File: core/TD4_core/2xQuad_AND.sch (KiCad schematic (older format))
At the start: 2 parts, among them U18 74HC21

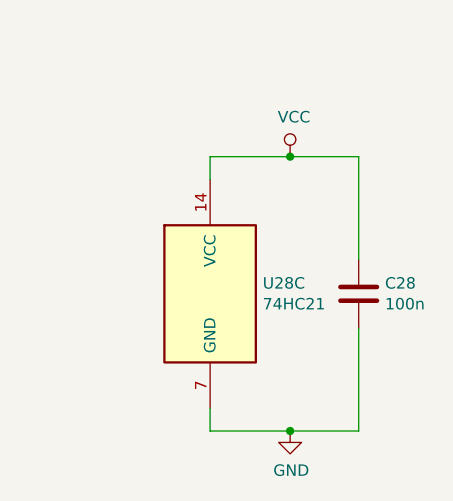
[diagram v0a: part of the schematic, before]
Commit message: Core schematic done. Backplane connector added, including separate .sch file to append.
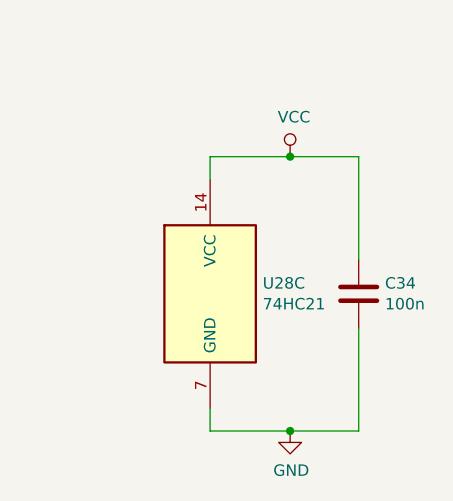
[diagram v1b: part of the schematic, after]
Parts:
- C24: renamed from C18; footprint (none) -> Capacitor_SMD:C_0805_2012Metric
- U18: footprint (none) -> Package_SO:SOIC-14_3.9x8.7mm_P1.27mm
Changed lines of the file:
@@
 encoding utf-8
 Sheet 7 23
-Title ""
+Title "TD4 core module"
 Date ""
-Rev ""
+Rev "v1.0"
 Comp ""
 Comment1 ""
@@
 F 0 "U28" H 4950 2875 50  0000 C CNN
 F 1 "74HC21" H 4950 2784 50  0000 C CNN
-F 2 "" H 4950 2500 50  0001 C CNN
+F 2 "Package_SO:SOIC-14_3.9x8.7mm_P1.27mm" H 4950 2500 50  0001 C CNN
 F 3 "http://www.ti.com/lit/gpn/sn74LS21" H 4950 2500 50  0001 C CNN
 	1    4950 2500
@@
 F 0 "U28" H 4950 3925 50  0000 C CNN
 F 1 "74HC21" H 4950 3834 50  0000 C CNN
-F 2 "" H 4950 3550 50  0001 C CNN
+F 2 "Package_SO:SOIC-14_3.9x8.7mm_P1.27mm" H 4950 3550 50  0001 C CNN
 F 3 "http://www.ti.com/lit/gpn/sn74LS21" H 4950 3550 50  0001 C CNN
 	2    4950 3550
@@
 F 0 "U28" H 8280 5546 50  0000 L CNN
 F 1 "74HC21" H 8280 5455 50  0000 L CNN
-F 2 "" H 8050 5500 50  0001 C CNN
+F 2 "Package_SO:SOIC-14_3.9x8.7mm_P1.27mm" H 8050 5500 50  0001 C CNN
 F 3 "http://www.ti.com/lit/gpn/sn74LS21" H 8050 5500 50  0001 C CNN
 	3    8050 5500
@@
 AR Path="/5C5DC05E/5CD3CB5B/5C84DA33" Ref="C?"  Part="1"
 AR Path="/5C5DC05E/5CD3CB61/5C84DA33" Ref="C?"  Part="1"
-AR Path="/5C594F41/5C66871A/5C84DA33" Ref="C18"  Part="1"
+AR Path="/5C594F41/5C66871A/5C84DA33" Ref="C24"  Part="1"
 AR Path="/5C594F41/5C66DC99/5C84DA33" Ref="C?"  Part="1"
-AR Path="/5C594F41/5C66DD80/5C84DA33" Ref="C25"  Part="1"
-AR Path="/5C594F41/5C676674/5C84DA33" Ref="C28"  Part="1"
-F 0 "C28" H 8815 5546 50  0000 L CNN
+AR Path="/5C594F41/5C66DD80/5C84DA33" Ref="C31"  Part="1"
+AR Path="/5C594F41/5C676674/5C84DA33" Ref="C34"  Part="1"
+F 0 "C34" H 8815 5546 50  0000 L CNN
 F 1 "100n" H 8815 5455 50  0000 L CNN
-F 2 "" H 8738 5350 50  0001 C CNN
+F 2 "Capacitor_SMD:C_0805_2012Metric" H 8738 5350 50  0001 C CNN
 F 3 "~" H 8700 5500 50  0001 C CNN
 	1    8700 5500
@@
 AR Path="/5C5DC05E/5CD3CB5B/5C84DB98" Ref="#PWR?"  Part="1"
 AR Path="/5C5DC05E/5CD3CB61/5C84DB98" Ref="#PWR?"  Part="1"
-AR Path="/5C594F41/5C66871A/5C84DB98" Ref="#PWR062"  Part="1"
+AR Path="/5C594F41/5C66871A/5C84DB98" Ref="#PWR076"  Part="1"
 AR Path="/5C594F41/5C66DC99/5C84DB98" Ref="#PWR?"  Part="1"
-AR Path="/5C594F41/5C66DD80/5C84DB98" Ref="#PWR082"  Part="1"
-AR Path="/5C594F41/5C676674/5C84DB98" Ref="#PWR090"  Part="1"
-F 0 "#PWR090" H 8400 5850 50  0001 C CNN
+AR Path="/5C594F41/5C66DD80/5C84DB98" Ref="#PWR096"  Part="1"
+AR Path="/5C594F41/5C676674/5C84DB98" Ref="#PWR0104"  Part="1"
+F 0 "#PWR0104" H 8400 5850 50  0001 C CNN
 F 1 "GND" H 8405 5927 50  0000 C CNN
 F 2 "" H 8400 6100 50  0001 C CNN
@@
 AR Path="/5C5DC05E/5CD3CB5B/5C84DC2A" Ref="#PWR?"  Part="1"
 AR Path="/5C5DC05E/5CD3CB61/5C84DC2A" Ref="#PWR?"  Part="1"
-AR Path="/5C594F41/5C66871A/5C84DC2A" Ref="#PWR061"  Part="1"
+AR Path="/5C594F41/5C66871A/5C84DC2A" Ref="#PWR075"  Part="1"
 AR Path="/5C594F41/5C66DC99/5C84DC2A" Ref="#PWR?"  Part="1"
-AR Path="/5C594F41/5C66DD80/5C84DC2A" Ref="#PWR081"  Part="1"
-AR Path="/5C594F41/5C676674/5C84DC2A" Ref="#PWR089"  Part="1"
-F 0 "#PWR089" H 8400 4750 50  0001 C CNN
+AR Path="/5C594F41/5C66DD80/5C84DC2A" Ref="#PWR095"  Part="1"
+AR Path="/5C594F41/5C676674/5C84DC2A" Ref="#PWR0103"  Part="1"
+F 0 "#PWR0103" H 8400 4750 50  0001 C CNN
 F 1 "VCC" H 8417 5073 50  0000 C CNN
 F 2 "" H 8400 4900 50  0001 C CNN

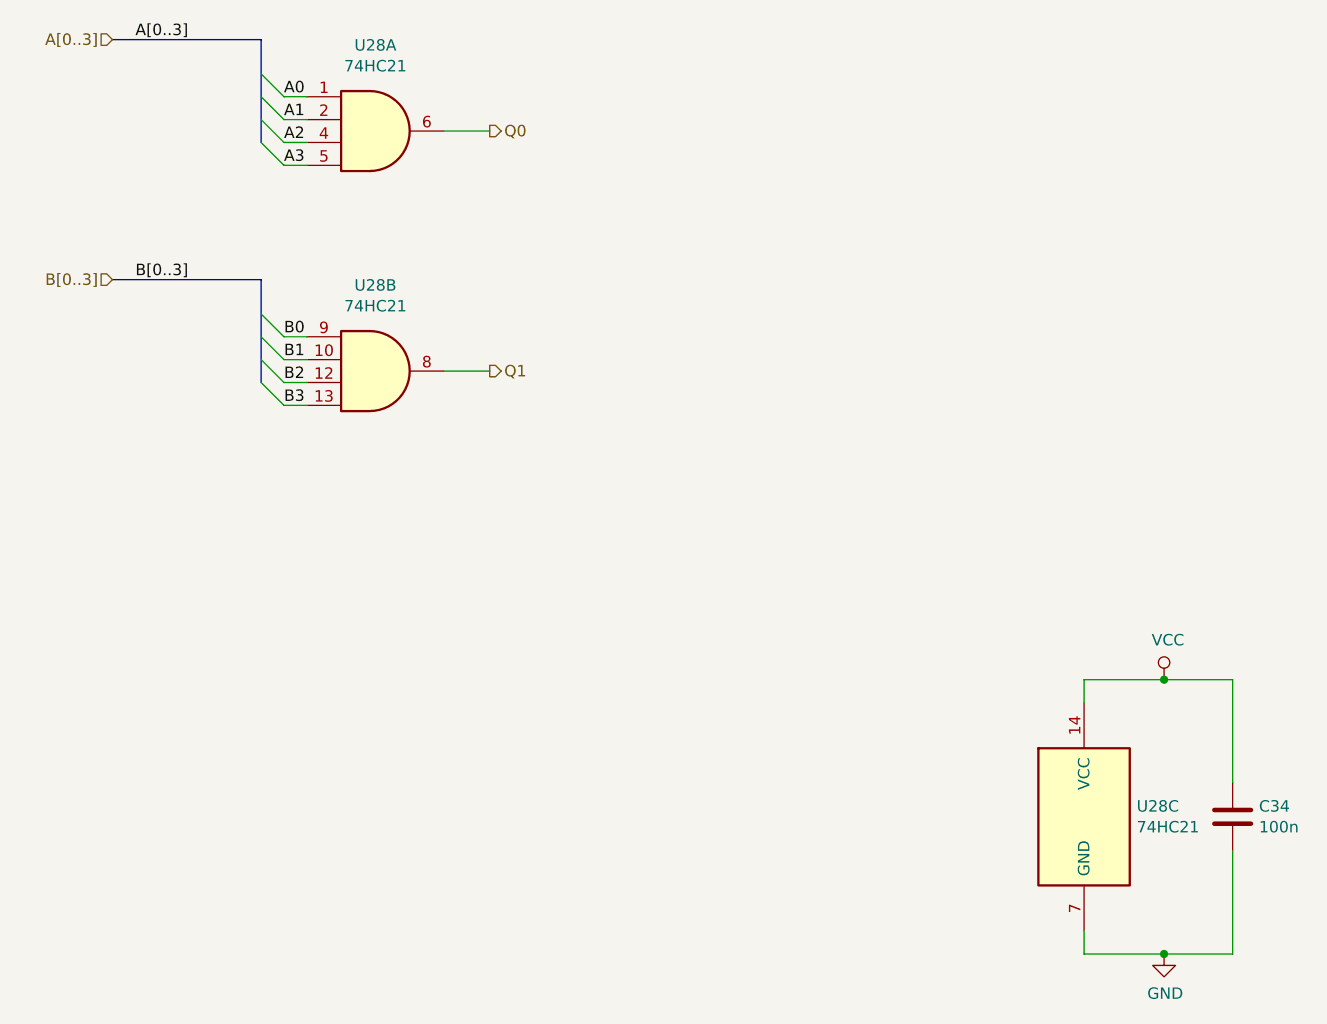
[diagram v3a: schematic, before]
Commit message: Replaced debug headers with vertical ones
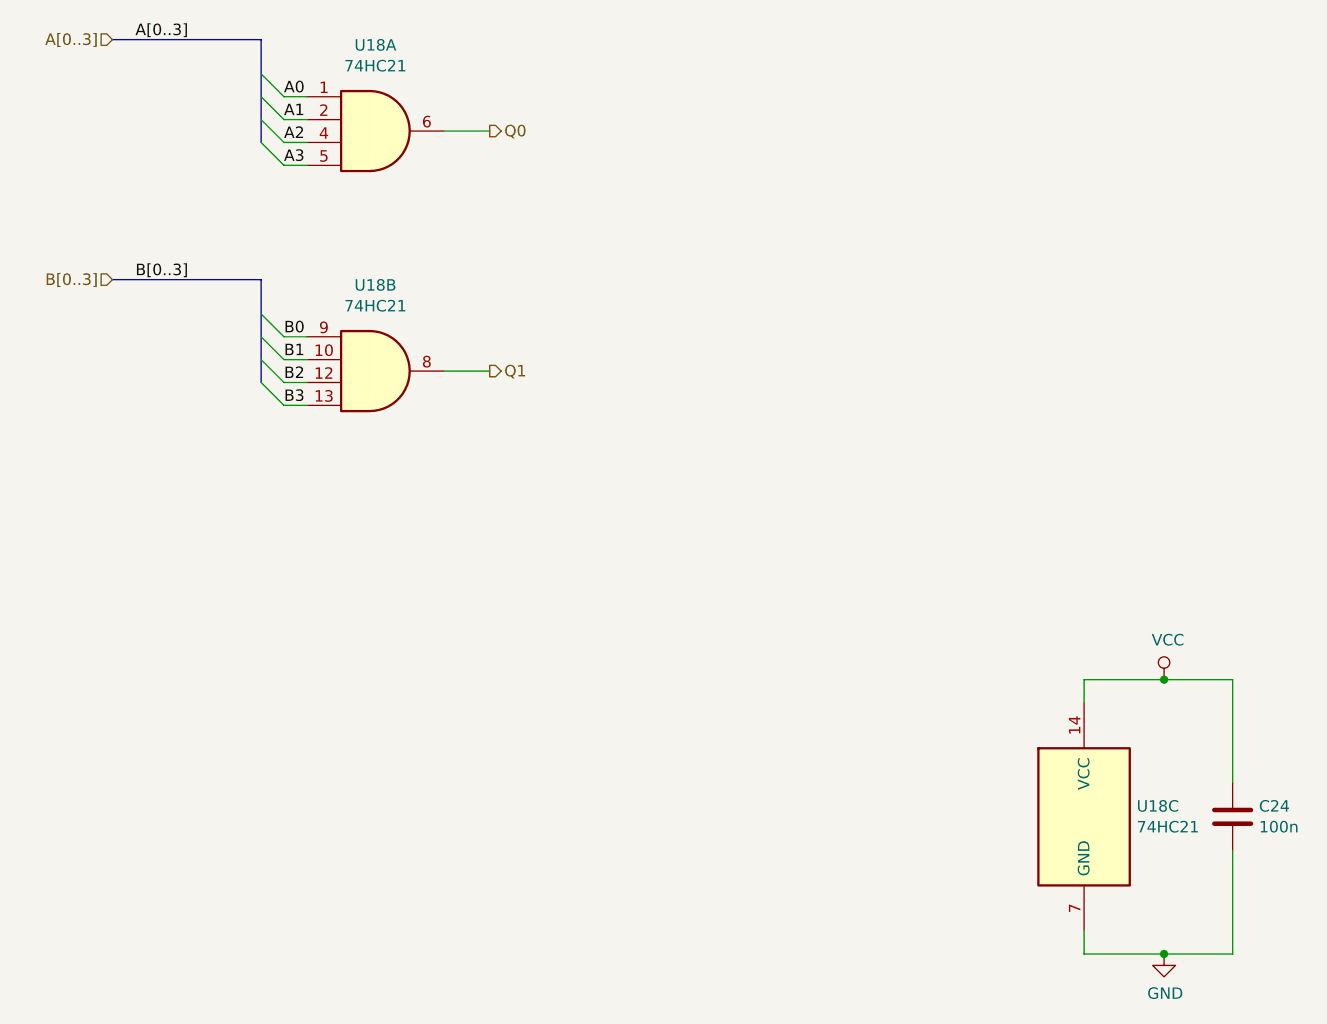
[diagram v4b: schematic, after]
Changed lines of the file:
@@
 AR Path="/5C594F41/5C66DD80/5C84D8AE" Ref="U25"  Part="1"
 AR Path="/5C594F41/5C676674/5C84D8AE" Ref="U28"  Part="1"
-F 0 "U28" H 4950 2875 50  0000 C CNN
+F 0 "U18" H 4950 2875 50  0000 C CNN
 F 1 "74HC21" H 4950 2784 50  0000 C CNN
 F 2 "Package_SO:SOIC-14_3.9x8.7mm_P1.27mm" H 4950 2500 50  0001 C CNN
@@
 AR Path="/5C594F41/5C66DD80/5C84D8EE" Ref="U25"  Part="2"
 AR Path="/5C594F41/5C676674/5C84D8EE" Ref="U28"  Part="2"
-F 0 "U28" H 4950 3925 50  0000 C CNN
+F 0 "U18" H 4950 3925 50  0000 C CNN
 F 1 "74HC21" H 4950 3834 50  0000 C CNN
 F 2 "Package_SO:SOIC-14_3.9x8.7mm_P1.27mm" H 4950 3550 50  0001 C CNN
@@
 AR Path="/5C594F41/5C66DD80/5C84D959" Ref="U25"  Part="3"
 AR Path="/5C594F41/5C676674/5C84D959" Ref="U28"  Part="3"
-F 0 "U28" H 8280 5546 50  0000 L CNN
+F 0 "U18" H 8280 5546 50  0000 L CNN
 F 1 "74HC21" H 8280 5455 50  0000 L CNN
 F 2 "Package_SO:SOIC-14_3.9x8.7mm_P1.27mm" H 8050 5500 50  0001 C CNN
@@
 AR Path="/5C594F41/5C66DD80/5C84DA33" Ref="C31"  Part="1"
 AR Path="/5C594F41/5C676674/5C84DA33" Ref="C34"  Part="1"
-F 0 "C34" H 8815 5546 50  0000 L CNN
+F 0 "C24" H 8815 5546 50  0000 L CNN
 F 1 "100n" H 8815 5455 50  0000 L CNN
 F 2 "Capacitor_SMD:C_0805_2012Metric" H 8738 5350 50  0001 C CNN
